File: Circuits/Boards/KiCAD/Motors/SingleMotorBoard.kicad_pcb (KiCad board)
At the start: 2 copper layers, 90.2 x 90.2 mm, 48 parts, among them J1 Conn_01x05, J2 Conn_01x01, J3 Conn_01x01, J4 Conn_01x01, J5 Conn_01x01, J6 Conn_01x01, J7 Conn_01x01, Q1 2N3904, Q10 Q_NMOS_DGS, Q11 Q_NMOS_DGS, Q12 Q_NMOS_DGS, Q13 Q_NMOS_DGS, Q2 2N3904, Q3 2N3904, Q4 2N3904, Q5 2N3904, Q6 2N3904, Q7 2N3904, Q8 2N3904, Q9 2N3904

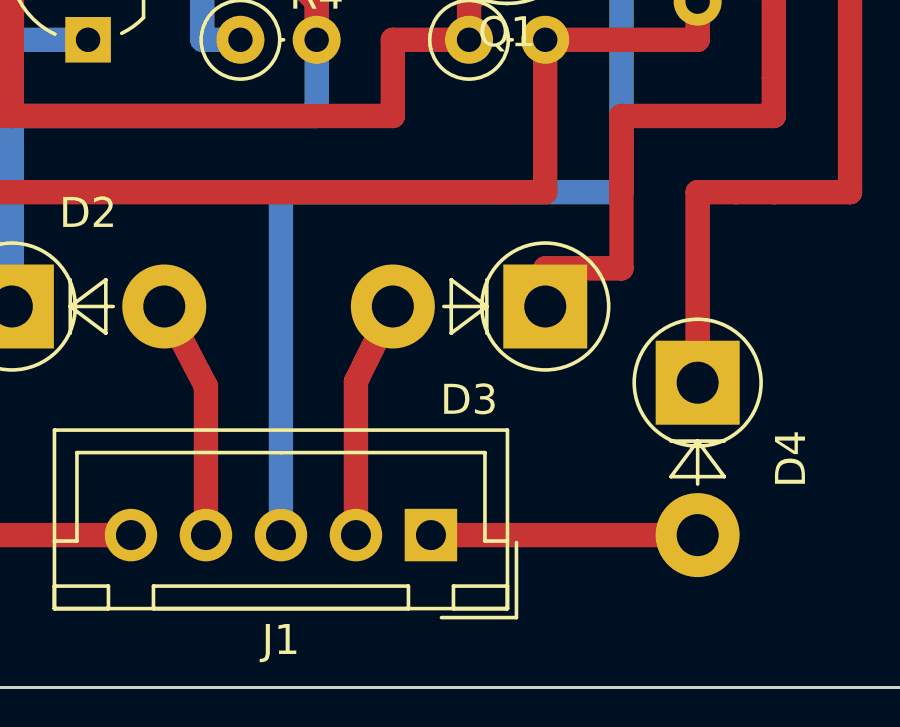
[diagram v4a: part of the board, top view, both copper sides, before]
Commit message: Created subcircuit for motor control and routing dual controller
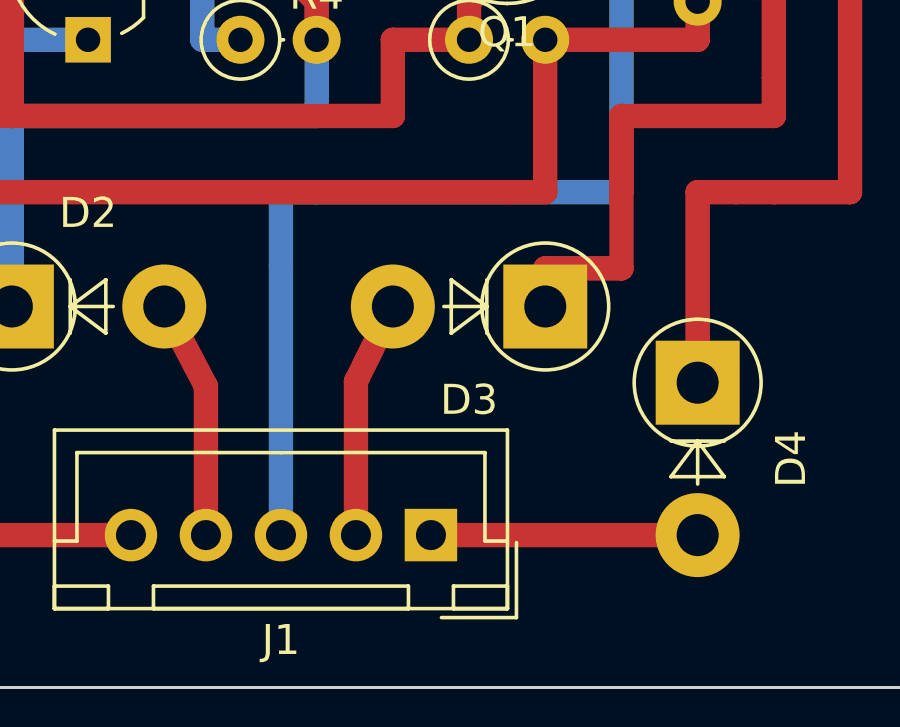
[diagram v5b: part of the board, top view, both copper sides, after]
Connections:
- net /BBM renamed /MotorControlUnit/BBM
- net /Dir renamed /MotorControlUnit/Dir
- net /FBM renamed /MotorControlUnit/FBM
- net /MBB renamed /MotorControlUnit/MBB
- net /MBF renamed /MotorControlUnit/MBF
- net /MFB renamed /MotorControlUnit/MFB
- net /MFF renamed /MotorControlUnit/MFF
- net /Speed renamed /MotorControlUnit/Speed
- net /VG renamed /MotorControlUnit/VG
- net /VSW renamed /MotorControlUnit/VSW
- net /iSpeed renamed /MotorControlUnit/iSpeed
- net Net-(J3-Pad1) renamed +15V
